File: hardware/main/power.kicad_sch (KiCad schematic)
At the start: 43 parts, among them J1 USB-307HB-B-SU, J12 Interrupteur, J2 Conn_01x02, Q1 AO3401A, Q2 2N7002, U10 FS8205, U12 USBLC6-2SC6, U5 AP2112M-3.3, U6 AP2112K-3.3, U7 MT3608, U8 BQ24075RGTR, U9 DW01A

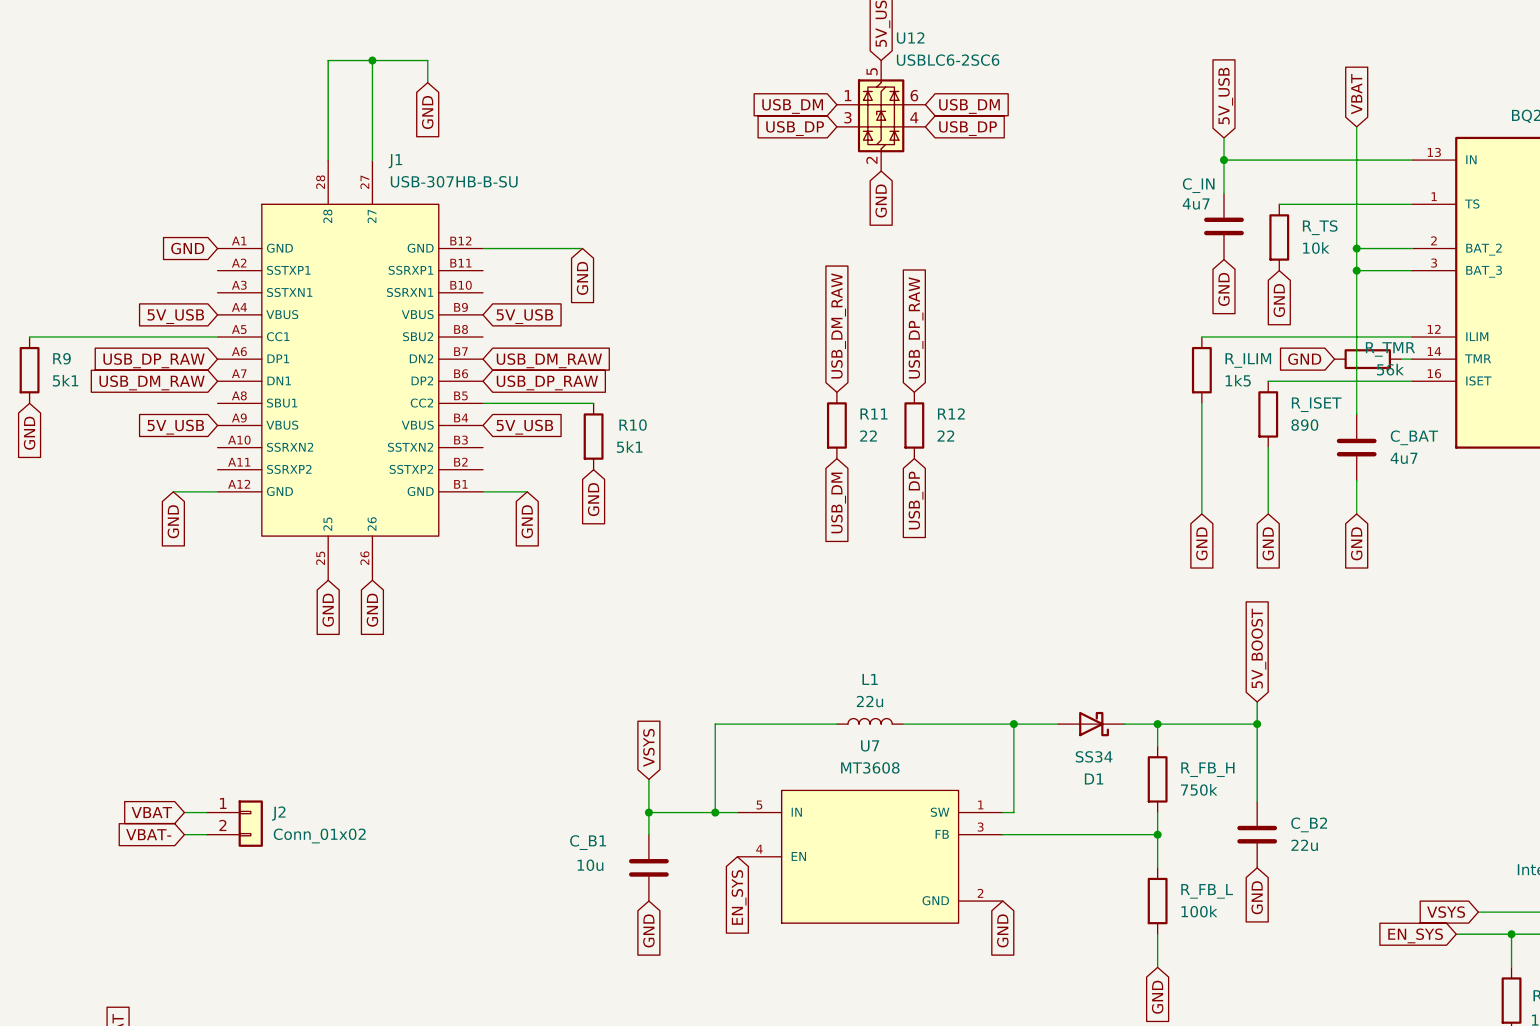
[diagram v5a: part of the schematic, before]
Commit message: hardware(power): J2 en 3 broches pour la NTC de la cellule 18650
Batterie retenue : cellule Li-ion 18650 de 3400-3500 mAh (et non plus une LiPo
pouch). Meme chimie, mais enveloppe acier avec event de surpression : plus
robuste dans un objet concu pour etre secoue et retourne. Une seule cellule —
deux auraient porte la charge a ~8 h, au-dela du pire cas du timer R_TMR qui
vient d'etre pose, et auraient impose de revoir R_ISET et R_ILIM.

- J2 : Conn_01x02 -> Conn_01x03, descendu de 2,54 mm pour que les broches 1 et
  2 restent exactement sur leurs fils. Broche 3 -> nouveau net BAT_TS.
  Empreinte JST_PH_B3B-PH-K_1x03_P2.00mm_Vertical (verifiee).
- R_TS (10k fixe) conservee mais passee en DNP : montee en meme temps que la
  NTC, elle fausse la mesure et le bq24075 suspend la charge SANS symptome
  visible. Monter l'une ou l'autre, jamais les deux, jamais aucune.
- Symbole Conn_01x03 repris de la bibliotheque KiCad officielle.

BOM realignee sur le schema, ou elle avait derive :
- elle attribuait J10 a la batterie alors que le schema utilise J2 depuis
  toujours — et j'avais cree un J10 pour le haut-parleur. J2 (batterie) et J10
  (haut-parleur) sont desormais tous deux listes correctement.
- ajout des composants introduits depuis l'audit et qui manquaient : FB3-FB6,
  R13/R14, C6/C7, R15-R19, R_TMR. Plus aucune reference du schema n'est
  absente de la BOM.
- J9 : la note citait « 32 LEDs = ~1,9 A » — c'est l'origine du chiffre du FSD.
  Remplacee par la limite reelle, qui vient du budget batterie et non du
  connecteur : ~8-10 LEDs externes.
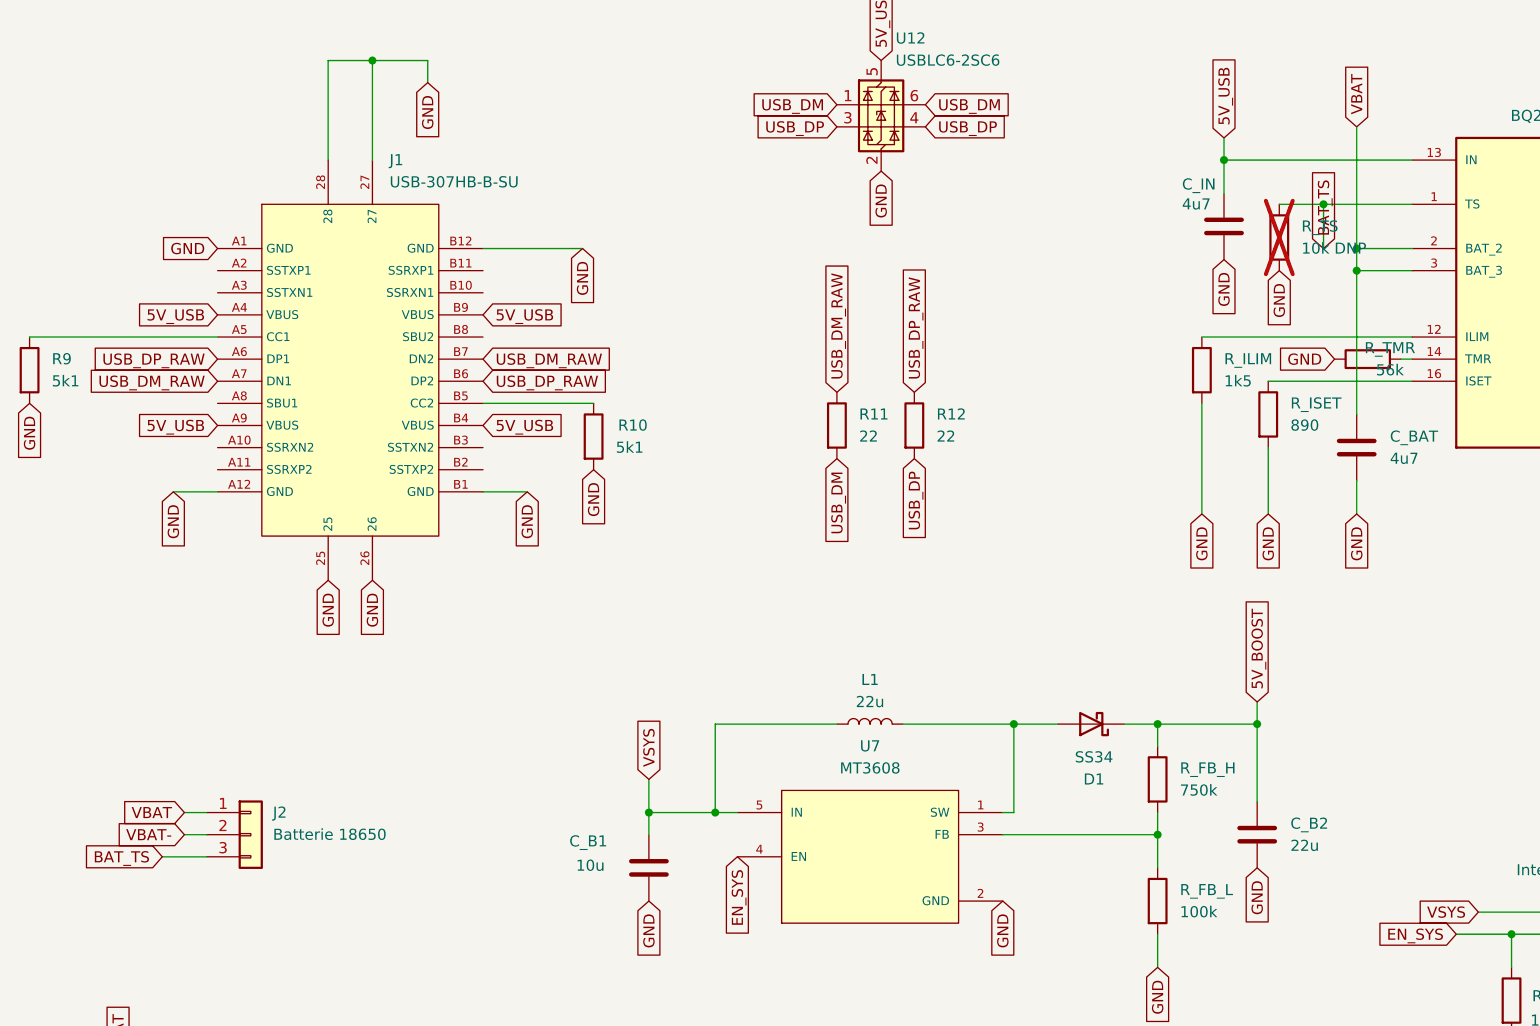
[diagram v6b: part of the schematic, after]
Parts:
- J2: value Conn_01x02 -> Batterie 18650; footprint Connector_JST:JST_PH_B2B-PH-K_1x02_P2.00mm_Vertical -> Connector_JST:JST_PH_B3B-PH-K_1x03_P2.00mm_Vertical; symbol Connector_Generic:Conn_01x02 -> Connector_Generic:Conn_01x03
- R_TS: value 10k -> 10k DNP; now not fitted
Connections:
- net BAT_TS: now reaches R_TS.1, U8.1 (TS)
- net BAT_TS: now also J2.3 (Pin_3)
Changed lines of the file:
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@@
 	)
 	(symbol
-		(lib_id "Connector_Generic:Conn_01x02")
-		(at 52.07 111.76 0)
+		(lib_id "Connector_Generic:Conn_01x03")
+		(at 52.07 114.3 0)
 		(unit 1)
 		(body_style 1)
@@
 			)
 		)
-		(property "Value" "Conn_01x02"
+		(property "Value" "Batterie 18650"
 			(at 54.61 114.2999 0)
 			(show_name no)
@@
 			)
 		)
-		(property "Footprint" "Connector_JST:JST_PH_B2B-PH-K_1x02_P2.00mm_Vertical"
-			(at 52.07 111.76 0)
+		(property "Footprint" "Connector_JST:JST_PH_B3B-PH-K_1x03_P2.00mm_Vertical"
+			(at 52.07 114.3 0)
 			(hide yes)
 			(show_name no)
@@
 		)
 		(property "Datasheet" ""
-			(at 52.07 111.76 0)
+			(at 52.07 114.3 0)
 			(hide yes)
 			(show_name no)
@@
 		)
 		(property "Description" "Generic connector, single row, 01x02, script generated (kicad-library-utils/schlib/autogen/connector/)"
-			(at 52.07 111.76 0)
-			(hide yes)
-			(show_name no)
-			(do_not_autoplace no)
-			(effects
-				(font
-					(size 1.27 1.27)
-				)
-			)
+			(at 52.07 114.3 0)
+			(hide yes)
+			(show_name no)
+			(do_not_autoplace no)
+			(effects
+				(font
+					(size 1.27 1.27)
+				)
+			)
+		)
+		(pin "1"
 		)
 		(pin "2"
 		)
-		(pin "1"
+		(pin "3"
 		)
 		(instances
@@
 		(on_board yes)
 		(in_pos_files yes)
-		(dnp no)
+		(dnp yes)
 		(fields_autoplaced yes)
 		(property "Reference" "R_TS"
@@
 			)
 		)
-		(property "Value" "10k"
+		(property "Value" "10k DNP"
 			(at 172.72 46.9899 0)
 			(show_name no)
@@
 		(color 0 0 0 0)
 	)
+	(wire
+		(pts
+			(xy 46.99 116.84) (xy 41.91 116.84)
+		)
+		(stroke
+			(width 0)
+			(type default)
+		)
+	)
+	(global_label "BAT_TS"
+		(shape input)
+		(at 41.91 116.84 180)
+		(fields_autoplaced yes)
+		(effects
+			(font
+				(size 1.27 1.27)
+			)
+			(justify right)
+		)
+		(property "Intersheetrefs" "${INTERSHEET_REFS}"
+			(at 30.479999999999997 116.84 0)
+			(hide yes)
+			(show_name no)
+			(do_not_autoplace no)
+			(effects
+				(font
+					(size 1.27 1.27)
+				)
+				(justify right)
+			)
+		)
+	)
+	(junction
+		(at 175.26 41.91)
+		(diameter 0)
+		(color 0 0 0 0)
+	)
+	(wire
+		(pts
+			(xy 175.26 41.91) (xy 175.26 46.99)
+		)
+		(stroke
+			(width 0)
+			(type default)
+		)
+	)
+	(global_label "BAT_TS"
+		(shape input)
+		(at 175.26 46.99 270)
+		(fields_autoplaced yes)
+		(effects
+			(font
+				(size 1.27 1.27)
+			)
+			(justify left)
+		)
+		(property "Intersheetrefs" "${INTERSHEET_REFS}"
+			(at 186.69 46.99 0)
+			(hide yes)
+			(show_name no)
+			(do_not_autoplace no)
+			(effects
+				(font
+					(size 1.27 1.27)
+				)
+				(justify left)
+			)
+		)
+	)
 )

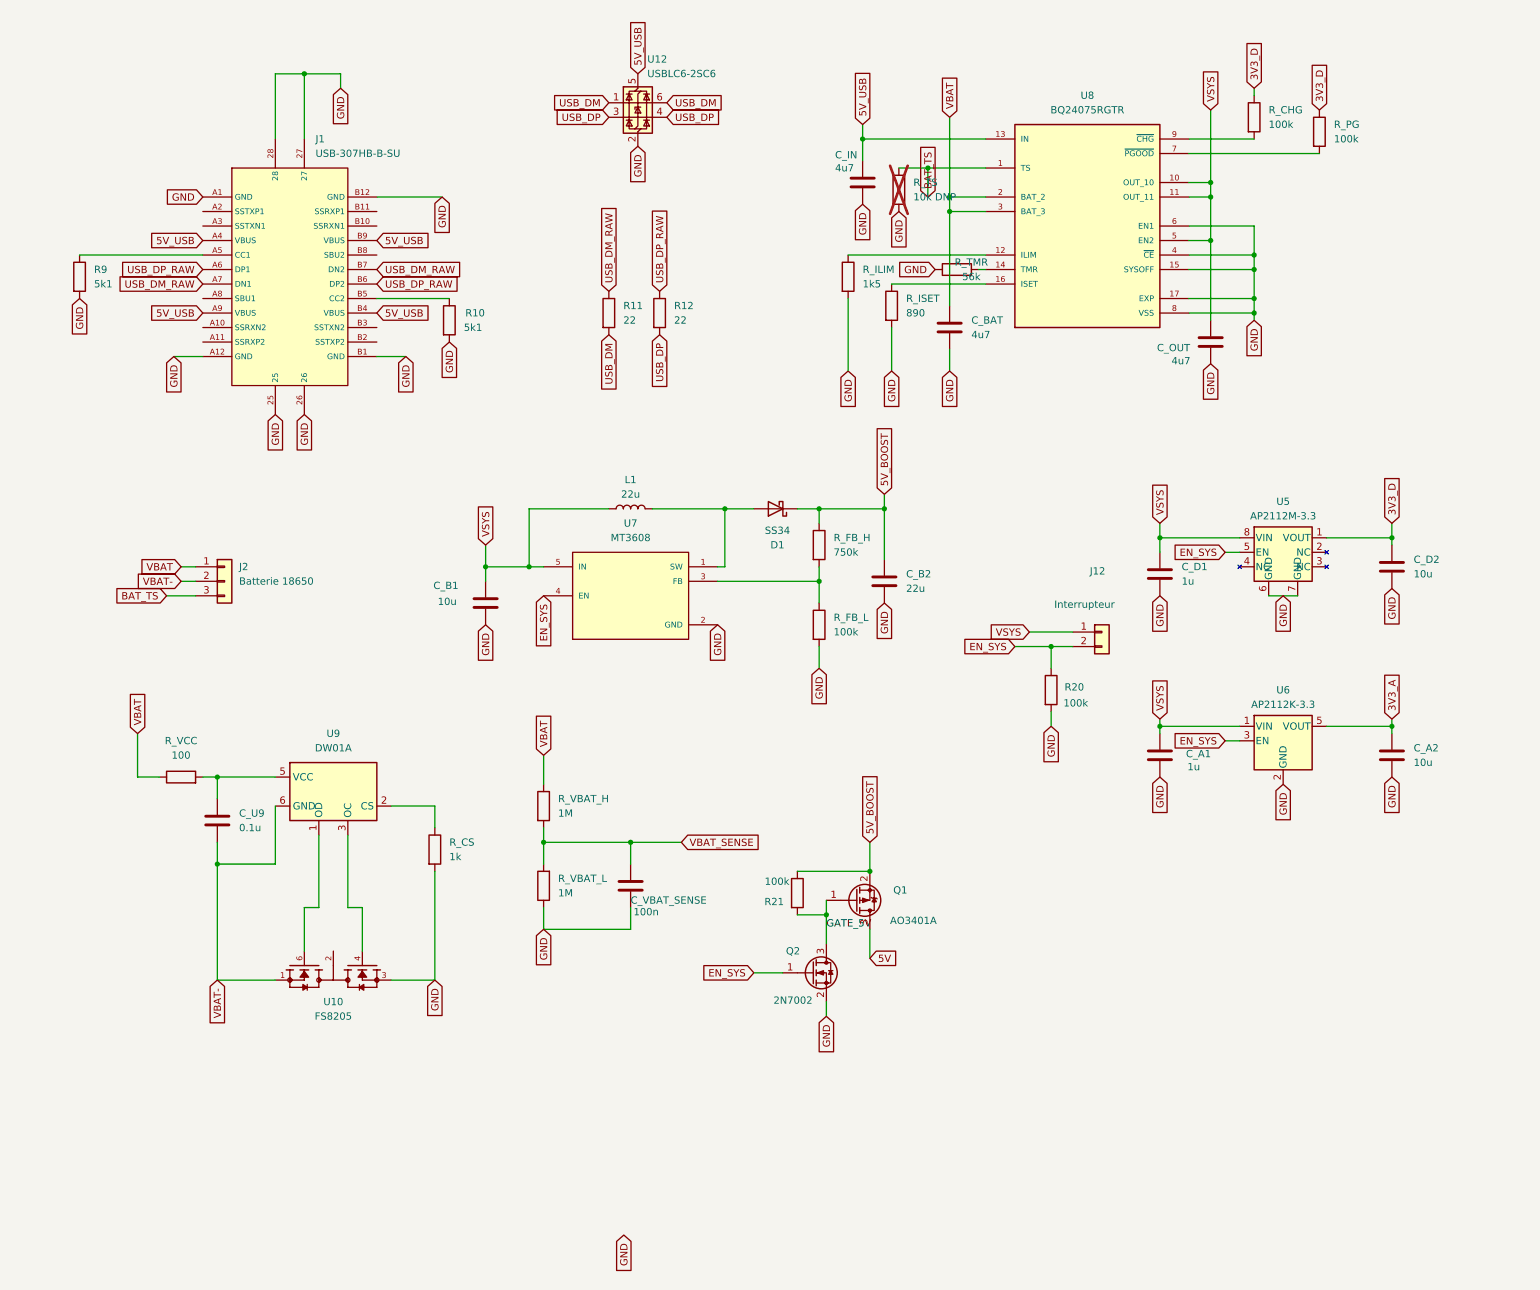
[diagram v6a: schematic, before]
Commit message: hardware: 48 erreurs ERC traitees, 22 points de test poses, VBAT_SENSE retire de J8.5
Les rapports ERC precedents portaient « Report includes: Warnings » : les
erreurs en etaient exclues a l'export et le resume affichait « Errors 0 ».
Elles etaient donc presentes depuis le debut et je ne les ai pas vues — il faut
exporter avec les erreurs incluses.

48 erreurs, trois familles, toutes des faux positifs au sens electrique mais
qu'il faut declarer sinon l'ERC reste inexploitable :

1. power_pin_not_driven (14) : le projet n'utilise aucun symbole d'alimentation,
   les rails sont des global labels, et KiCad exige qu'un net « power input »
   soit pilote par une pin « power output ». Nine PWR_FLAG poses, un par rail
   (GND, VSYS, VBAT, VBAT-, 3V3_D, 3V3_A, 5V, 5V_BOOST, 5V_USB).
2. pin_not_connected (29) : broches volontairement libres — paires SuperSpeed et
   SBU de l'USB-C (design USB 2.0), UART0 et IO35-37 de l'ESP32 (reserves a la
   PSRAM octale), GPIO du PCM5122, interruptions de l'IMU, reserves de
   connecteurs, drains communs du FS8205. Marqueurs no_connect.
3. divers (5) : label GND orphelin hors page (122, 228.81 — la page fait
   210 mm de haut) supprime ; C1_AV/C2_DV/C3_CP renommes C_AVDD/C_DVDD/C_CPVDD
   (KiCad lit « C1_AV » comme un prefixe suivi de « 1_AV », donc non annote) ;
   OUT_11 du bq24075 passee en passive (les deux broches sont la meme sortie).

Points de test : les 22 valides sont poses, chacun relie par un fil court a un
global label (le routeur les placera ou ils sont accessibles). 22/22 verifies
sur leur net. Trois nets anonymes nommes au passage : BQ_ISET, BQ_CHG,
BOOST_FB. Avec les 4 existants, 26 points de test.

VBAT_SENSE retire de J8.5 : noeud ADC haute impedance (1M // 1M) sorti dans un
cable, sans usage cote face avant depuis que les analogiques passent par
l'ADS7830. Broche marquee non connectee.

CORRECTION D'OUTIL : tools/kicad_netlist.py comptait PWR_FLAG comme un nom de
net, ce qui faisait fusionner les neuf rails en un seul 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
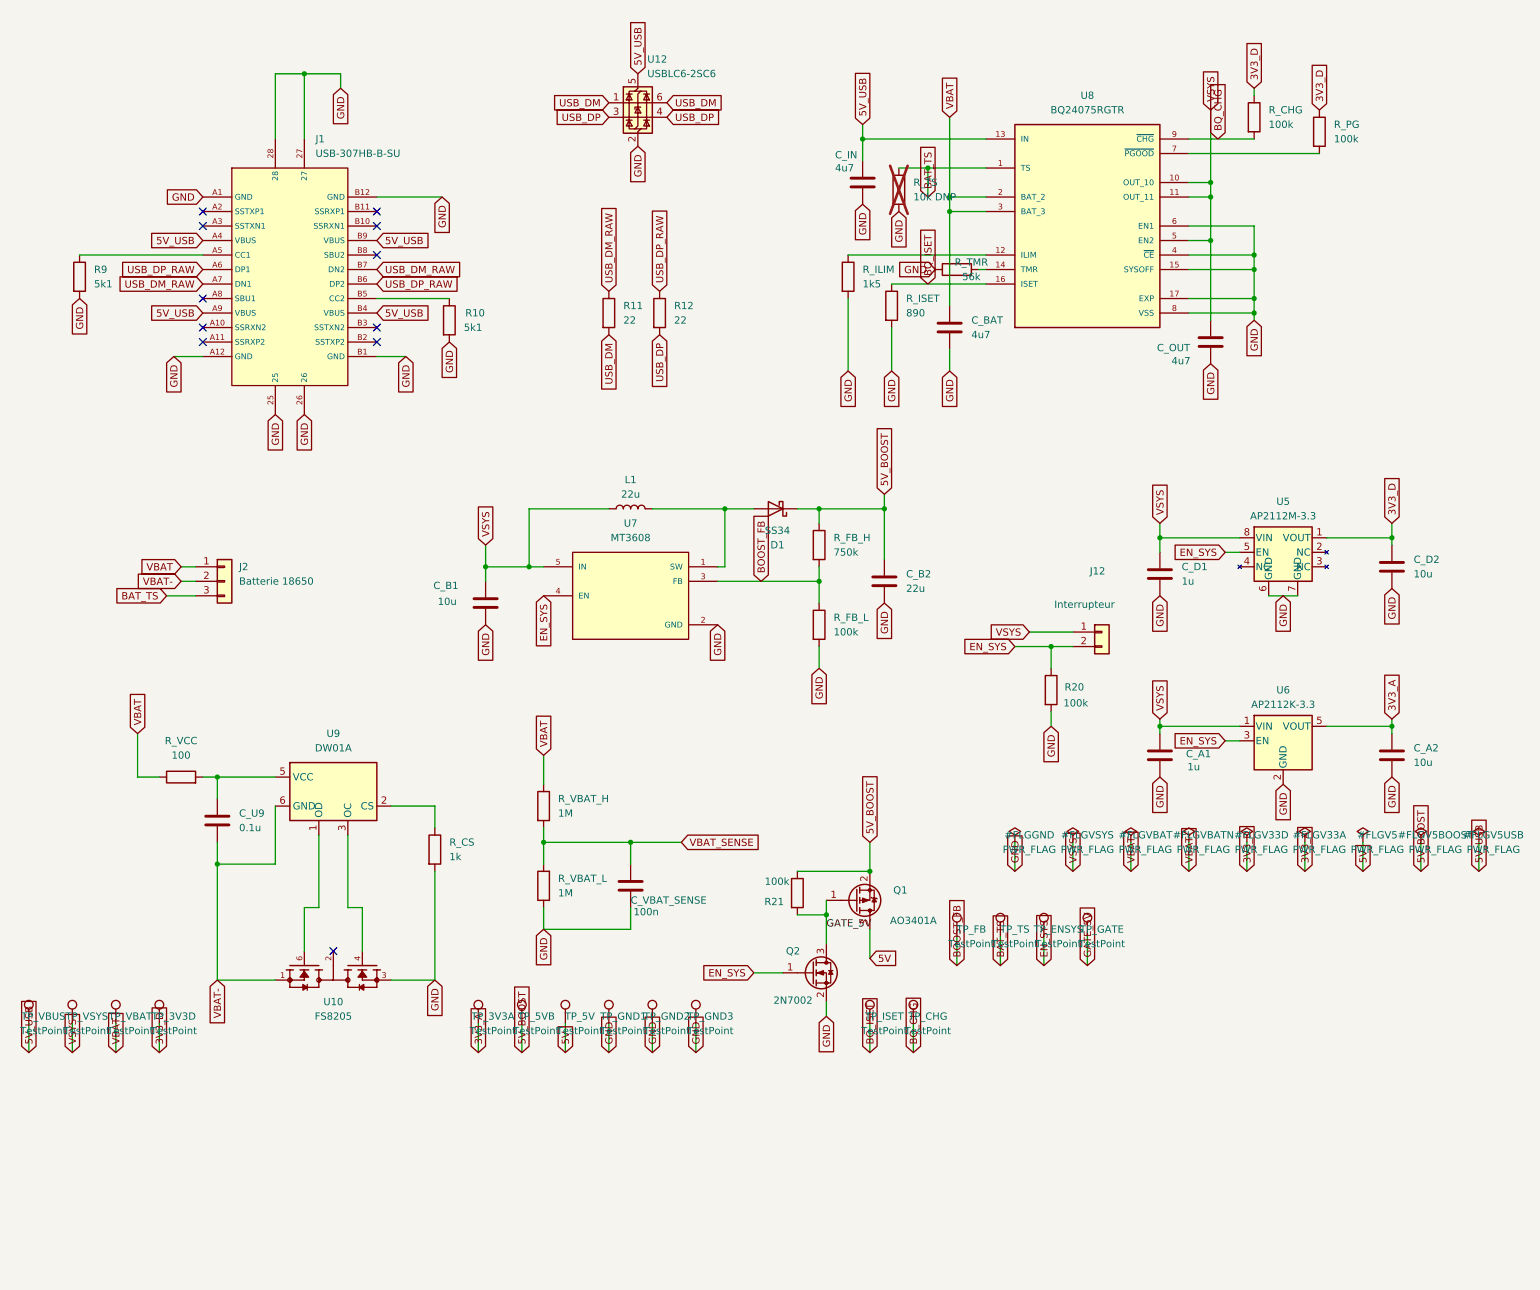
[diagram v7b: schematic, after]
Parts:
- added TP_3V3A, TP_3V3D, TP_5V, TP_5VB, TP_CHG, TP_ENSYS, TP_FB, TP_GATE, TP_GND1, TP_GND2, TP_GND3, TP_ISET, TP_TS, TP_VBAT, TP_VBUS, TP_VSYS: TestPoint, TestPoint:TestPoint_Pad_D1.5mm, symbol Connector:TestPoint
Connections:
- net 3V3_A: now also TP_3V3A.1
- net 3V3_D: now also TP_3V3D.1
- net 5V: now also TP_5V.1
- net 5V_BOOST: now also TP_5VB.1
- net 5V_USB: now also TP_VBUS.1
- net BAT_TS: now also TP_TS.1
- net EN_SYS: now also TP_ENSYS.1
- net GATE_5V: now also TP_GATE.1
- net GND: now also TP_GND1.1, TP_GND2.1, TP_GND3.1
- net VBAT: now also TP_VBAT.1
- net VSYS: now also TP_VSYS.1
- net BOOST_FB: now reaches R_FB_H.2, R_FB_L.1, U7.3 (FB)
- net BOOST_FB: now also TP_FB.1
- net BQ_CHG: now reaches R_CHG.2, U8.9 (~{CHG})
- net BQ_CHG: now also TP_CHG.1
- net BQ_ISET: now reaches R_ISET.1, U8.16 (ISET)
- net BQ_ISET: now also TP_ISET.1
- no-connect marks 0 -> 11
